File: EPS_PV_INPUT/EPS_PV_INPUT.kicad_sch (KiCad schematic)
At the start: 17 parts, among them J6501 PV, J6502 PV, J6503 PV, J6504 PV, J6505 PV, J6506 PV, J6507 VBUS

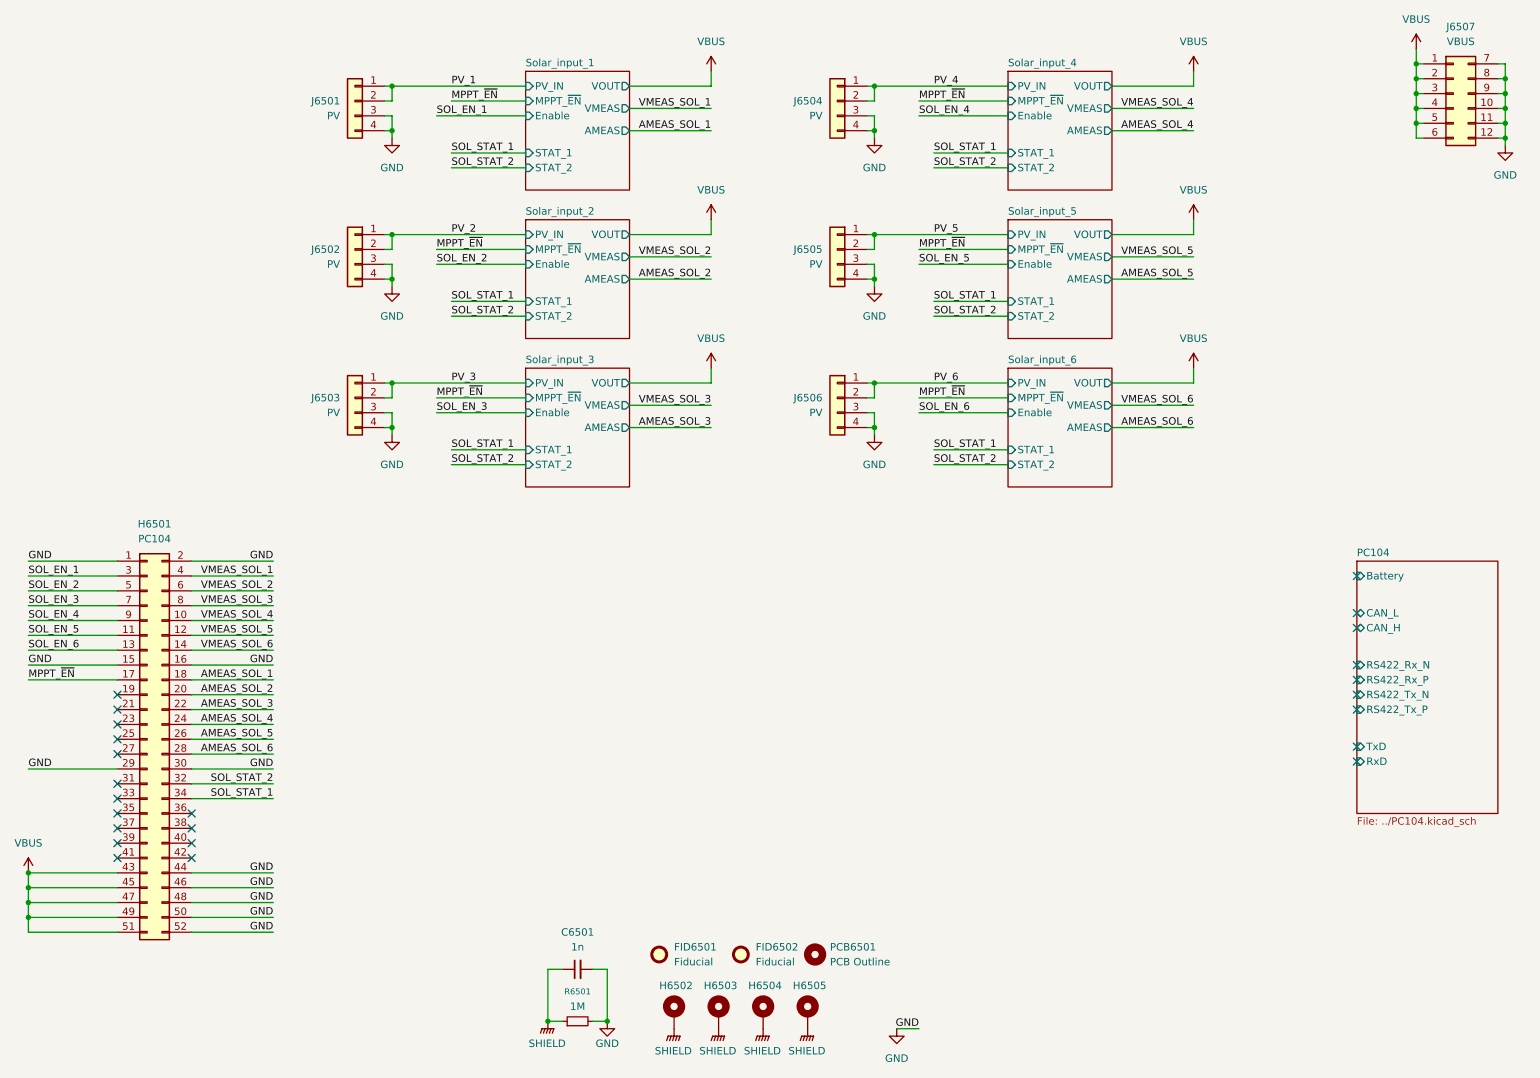
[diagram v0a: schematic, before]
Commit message: pcb progres for all components
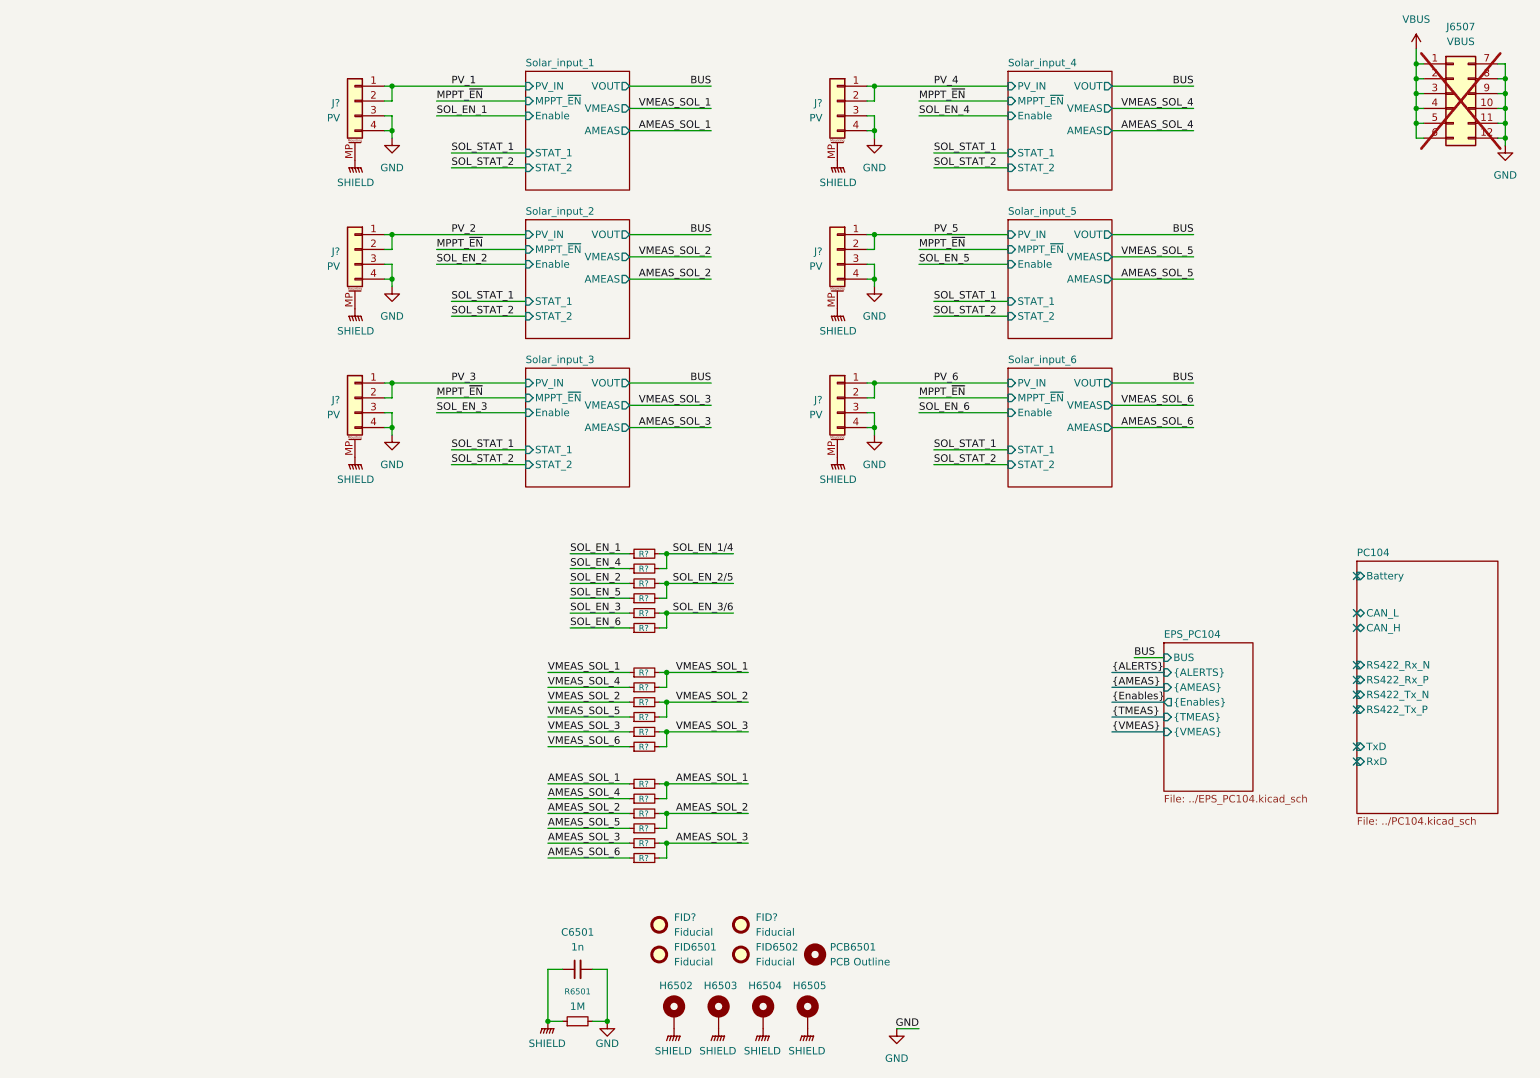
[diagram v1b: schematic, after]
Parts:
- removed H6501: PC104, Connector_PinSocket_2.54mm:PinSocket_2x26_P2.54mm_Vertical, symbol Connector_Generic:Conn_02x26_Odd_Even
- removed J6501, J6502, J6503, J6504, J6505, J6506: PV, Connector_Molex:Molex_CLIK-Mate_502494-0470_1x04-1MP_P2.00mm_Horizontal, symbol Connector_Generic:Conn_01x04
- added FID? (x2): Fiducial, Fiducial:Fiducial_1mm_Mask2mm, symbol Mechanical:Fiducial
- added J? (x6): PV, Connector_Molex:Molex_PicoBlade_53261-0471_1x04-1MP_P1.25mm_Horizontal, symbol Connector_Generic_MountingPin:Conn_01x04_MountingPin
- added R? (x18): 0, Resistor_SMD:R_0603_1608Metric_Pad0.98x0.95mm_HandSolder, symbol Device:R_Small
- J6507: now not fitted; now left out of the parts list
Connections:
- net AMEAS_SOL_1: now also R?.1, R?.2, R?.2
- net AMEAS_SOL_2: now also R?.1, R?.2, R?.2
- net AMEAS_SOL_3: now also R?.1, R?.2, R?.2
- net AMEAS_SOL_4: now also R?.1
- net AMEAS_SOL_5: now also R?.1
- net AMEAS_SOL_6: now also R?.1
- net GND: now also J?.3 (Pin_3), J?.3 (Pin_3), J?.3 (Pin_3), J?.3 (Pin_3), J?.3 (Pin_3), J?.3 (Pin_3), J?.4 (Pin_4), J?.4 (Pin_4), J?.4 (Pin_4), J?.4 (Pin_4), J?.4 (Pin_4), J?.4 (Pin_4)
- net PV_1: now also J?.1 (Pin_1), J?.2 (Pin_2)
- net PV_2: now also J?.1 (Pin_1), J?.2 (Pin_2)
- net PV_3: now also J?.1 (Pin_1), J?.2 (Pin_2)
- net PV_4: now also J?.1 (Pin_1), J?.2 (Pin_2)
- net PV_5: now also J?.1 (Pin_1), J?.2 (Pin_2)
- net PV_6: now also J?.1 (Pin_1), J?.2 (Pin_2)
- net SHIELD: now also J?.MP (MountPin), J?.MP (MountPin), J?.MP (MountPin), J?.MP (MountPin), J?.MP (MountPin), J?.MP (MountPin)
- net SOL_EN_1: now also R?.1
- net SOL_EN_2: now also R?.1
- net SOL_EN_3: now also R?.1
- net SOL_EN_4: now also R?.1
- net SOL_EN_5: now also R?.1
- net SOL_EN_6: now also R?.1
- net VMEAS_SOL_1: now also R?.1, R?.2, R?.2
- net VMEAS_SOL_2: now also R?.1, R?.2, R?.2
- net VMEAS_SOL_3: now also R?.1, R?.2, R?.2
- net VMEAS_SOL_4: now also R?.1
- net VMEAS_SOL_5: now also R?.1
- net VMEAS_SOL_6: now also R?.1
- new net SOL_EN_1/4: R?.2, R?.2
- new net SOL_EN_2/5: R?.2, R?.2
- new net SOL_EN_3/6: R?.2, R?.2
- no-connect marks 24 -> 9
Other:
- added sheet EPS_PC104 (../EPS_PC104.kicad_sch)
